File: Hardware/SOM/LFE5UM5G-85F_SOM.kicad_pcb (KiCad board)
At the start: 8 copper layers, 67.6 x 25.4 mm, 157 parts, among them J1 SODIMM-200_Split, U1 LFE5UM5G-85F, U2 AS4C256M16D3, U3 W25Q128JVP, U4 TPS62A02ADRL, U5 TPS62A02ADRL, U6 TPS62A02ADRL, U7 TPS62A02ADRL

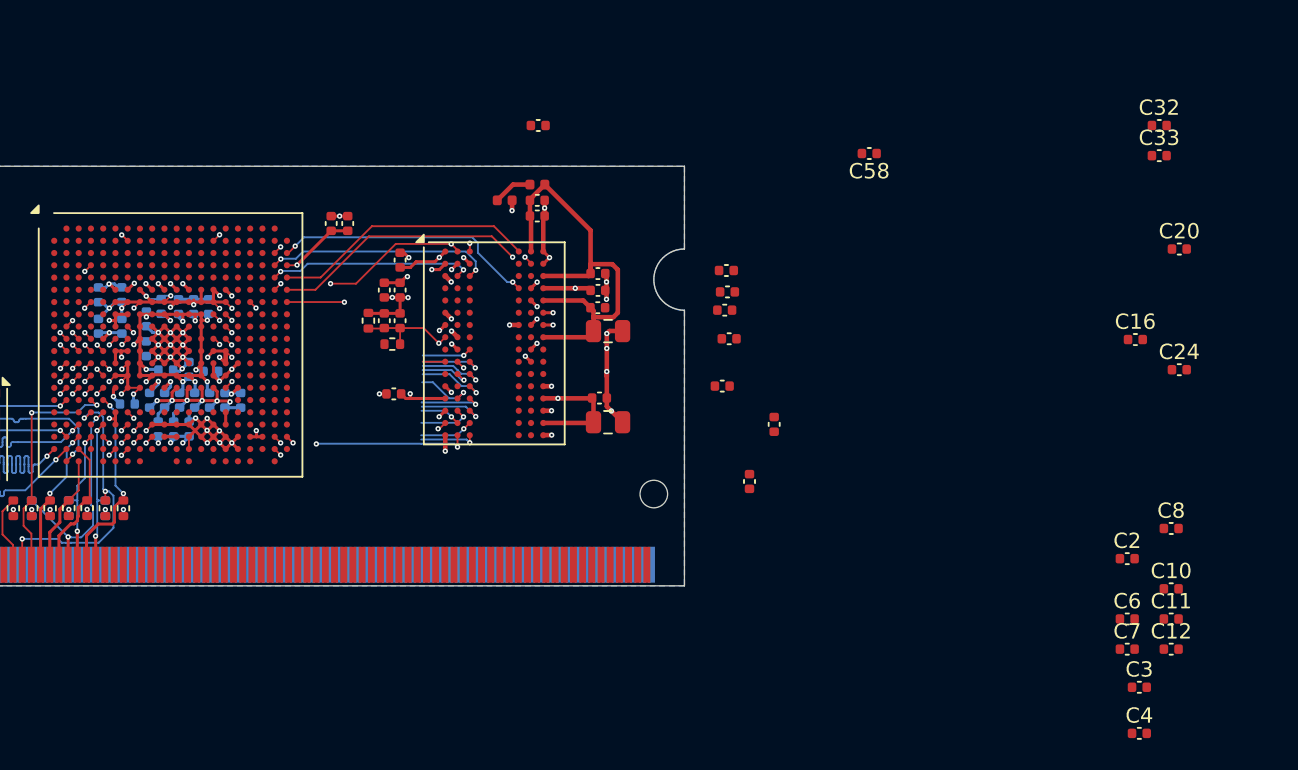
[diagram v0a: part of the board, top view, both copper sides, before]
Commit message: SOM: decoupling caps placement
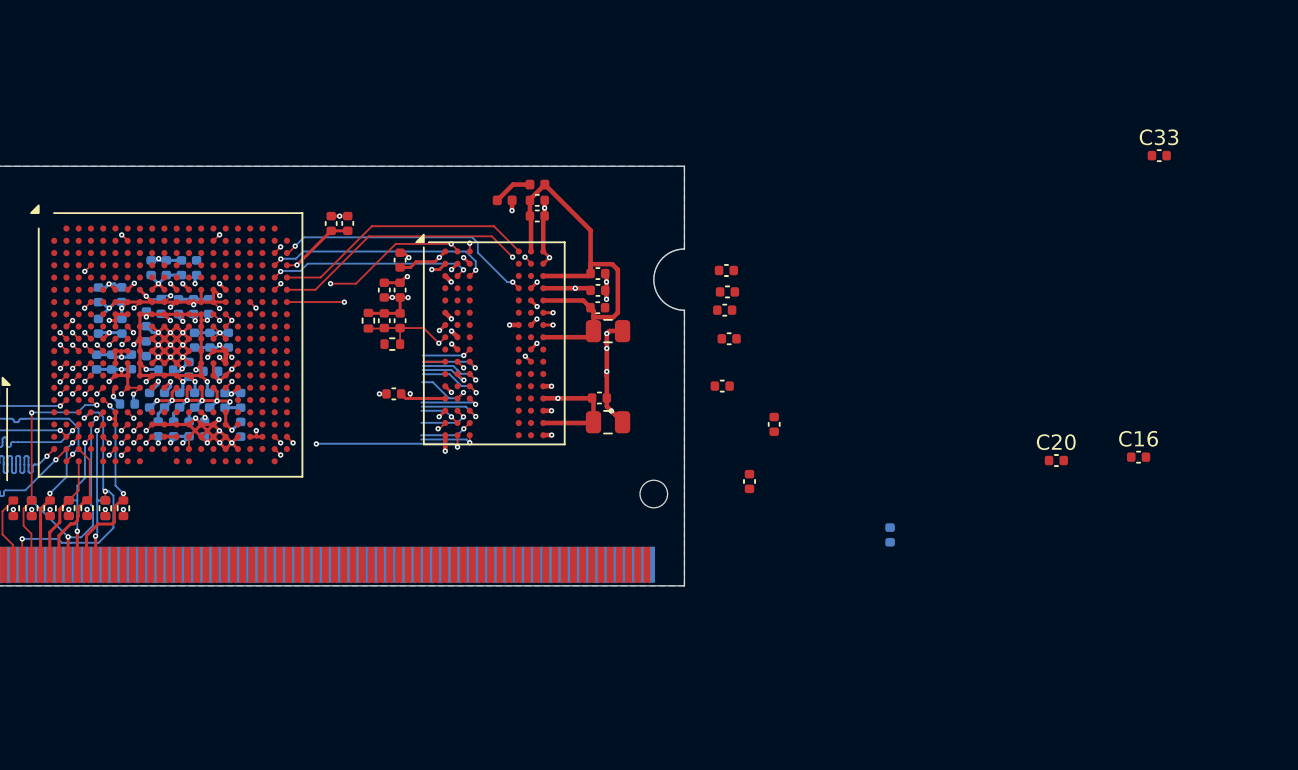
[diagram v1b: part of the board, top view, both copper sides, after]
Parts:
- C10, C11, C12, C2, C24, C3, C32, C4, C56, C58, C6, C7, C8: moved to B.Cu
- moved C4 72.3 mm to (111.1, 71.8), turned to 90 degrees
- moved C12 71.7 mm to (112.1, 71.8), turned to 90 degrees
- moved C8 68.8 mm to (113.3, 71.8), turned to 90 degrees
- moved C10 68.0 mm to (116.6, 65.6), turned to -90 degrees
- moved C6 67.8 mm to (114.6, 65.6), turned to -90 degrees
- moved C2 65.6 mm to (115.6, 65.6), turned to -90 degrees
- moved C11 65.4 mm to (118.5, 70.3), turned to -90 degrees
- moved C24 64.5 mm to (117.6, 65.6), turned to -90 degrees
- moved C7 64.2 mm to (117.5, 70.3), turned to -90 degrees
- moved C3 63.7 mm to (119.7, 70.3), turned to -90 degrees
- moved C58 47.0 mm to (118.1, 76.1), turned to 90 degrees
- moved C32 32.0 mm to (162.9, 83.0), turned to -90 degrees
- moved C56 27.8 mm to (120.5, 76.2), turned to 90 degrees
- moved C20 16.0 mm to (173.8, 78.2)
- moved C16 7.68 mm to (179.1, 78.0)
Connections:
- U1 pad L16: unconnected-(U1E-PR50A-PadL16) -> DDR_A4
- U1 pad L17: unconnected-(U1E-PR50B-PadL17) -> DDR_A5
- U1 pad L18: unconnected-(U1E-PR50C-PadL18) -> DDR_A6
- U1 pad L19: unconnected-(U1E-PR47C-PadL19) -> DDR_A2
- U1 pad L20: unconnected-(U1E-PR47A-PadL20) -> DDR_A0
- U1 pad M18: unconnected-(U1E-PR50D-PadM18) -> DDR_A7
- U1 pad M19: unconnected-(U1E-PR47D-PadM19) -> DDR_A3
- U1 pad M20: unconnected-(U1E-PR47B-PadM20) -> DDR_A1
- U1 pad N18: unconnected-(U1E-PR53C-PadN18) -> DDR_A8
- U1 pad P17: unconnected-(U1E-PR53D-PadP17) -> DDR_A9
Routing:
- net 1.5V: track 52.4 -> 61.4 mm, vias 9 -> 10
- net GND: track 208.0 -> 215.9 mm, vias 113 -> 110
- net VCCA1: track 0.80 -> 2.18 mm, vias 0 -> 1
- net 3.3V: track 55.1 -> 54.1 mm, vias 16 -> 15
- net VCC_SER_1: track 0.00 -> 0.81 mm, vias 0 -> 1
- net unconnected-(U1F-PL83B-PadN5): track 0.58 -> 0.00 mm, vias 1 -> 0
- net unconnected-(U1F-PL77A-PadM5): track 0.56 -> 0.01 mm, vias 1 -> 0

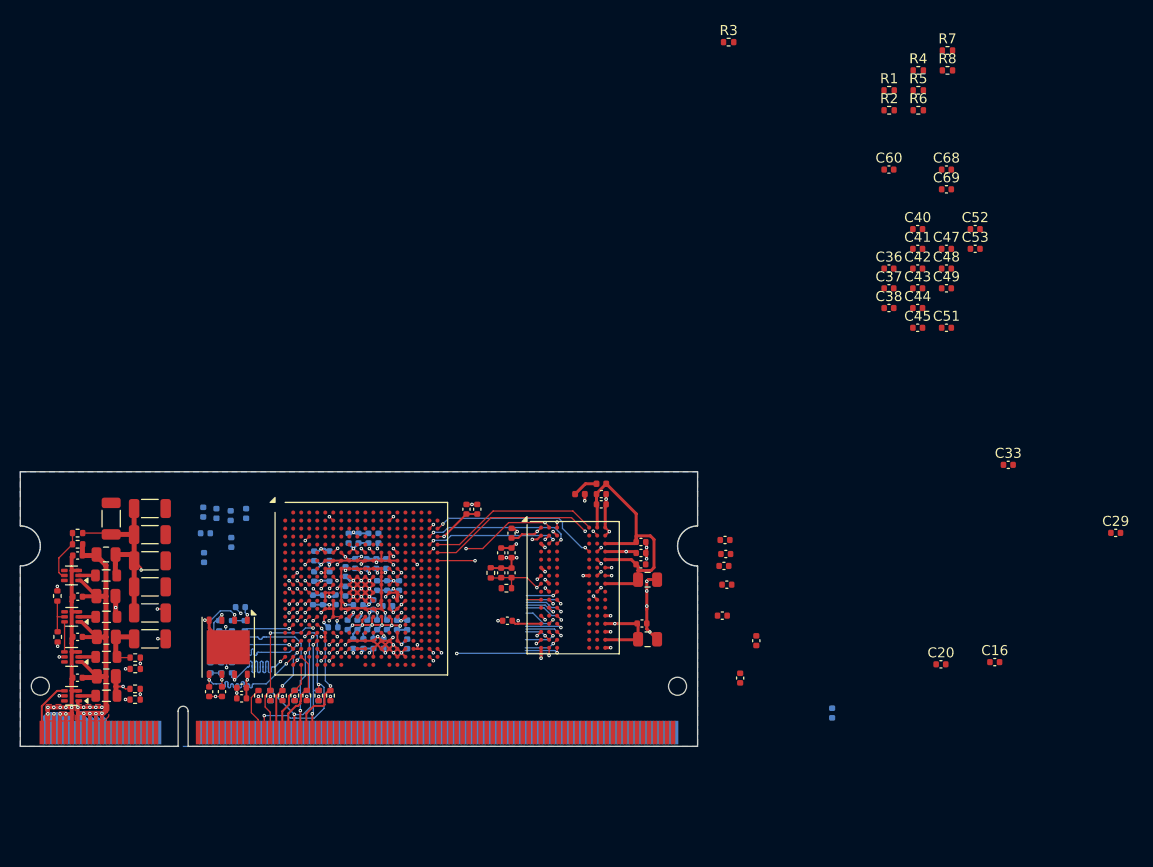
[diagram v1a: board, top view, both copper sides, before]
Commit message: SOM: more caps moved to their place
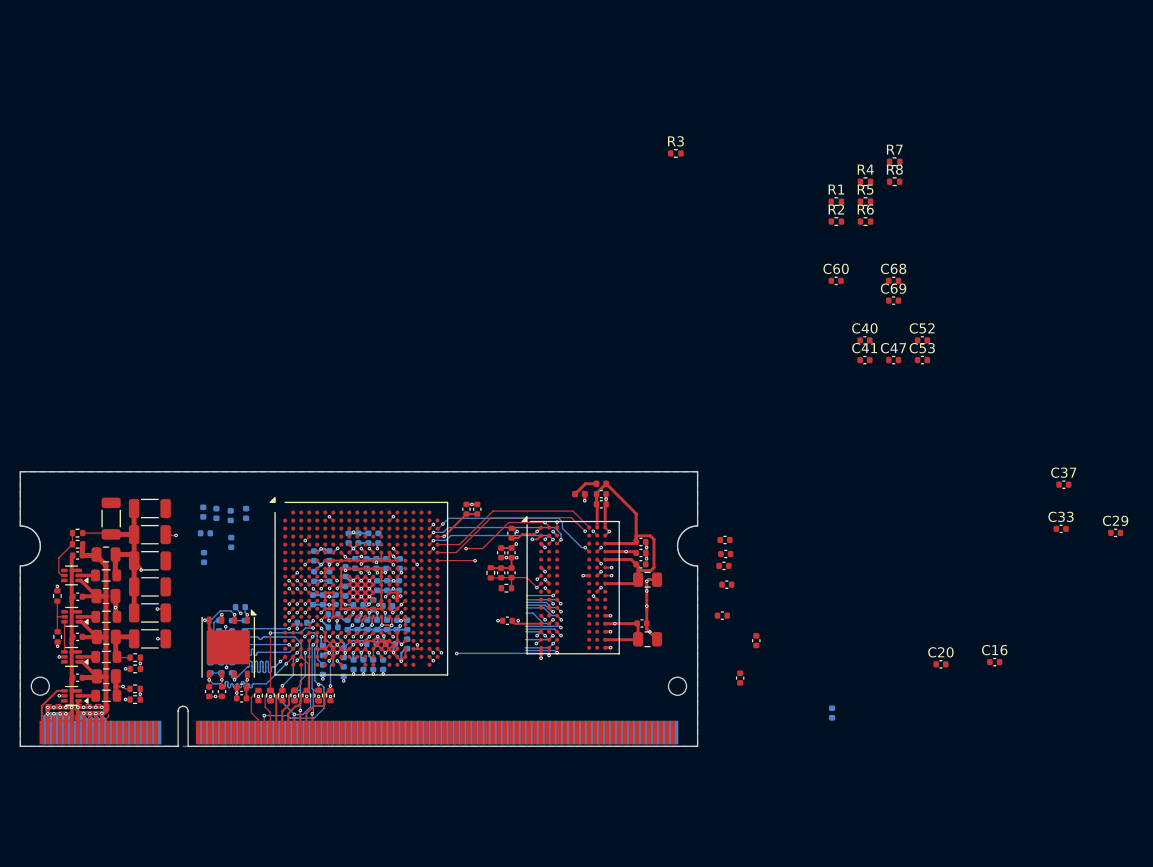
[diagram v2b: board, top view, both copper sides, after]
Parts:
- C36, C38, C42, C43, C44, C45, C48, C49, C51: moved to B.Cu
- moved C42 70.9 mm to (110.0, 74.0)
- moved C43 70.5 mm to (112.1, 78.7), turned to 90 degrees
- moved C51 70.1 mm to (112.1, 76.8), turned to 90 degrees
- moved C48 68.7 mm to (118.1, 78.2), turned to 90 degrees
- moved C44 67.8 mm to (114.2, 78.9), turned to 90 degrees
- moved C49 67.5 mm to (116.9, 76.2), turned to 180 degrees
- moved C45 65.8 mm to (114.2, 77.0), turned to 90 degrees
- moved C38 63.3 mm to (113.1, 73.2)
- moved C36 57.0 mm to (119.8, 68.1), turned to -90 degrees
- moved C37 26.2 mm to (186.0, 60.3)
- moved C68 12.3 mm to (169.0, 39.9)
- moved C40 12.3 mm to (166.2, 45.9)
- moved C41 12.3 mm to (166.2, 47.8)
- moved C47 12.3 mm to (169.0, 47.8)
- moved C52 12.3 mm to (171.9, 45.9)
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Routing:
- net VCCA1: track 2.18 -> 37.7 mm, vias 1 -> 2
- net VCCHTX0: track 0.56 -> 13.0 mm, vias 1 -> 4
- net GND: track 215.9 -> 227.6 mm, vias 110 -> 113
- net VCC_SER_0: track 0.00 -> 9.90 mm, vias 0 -> 3
- net VCC_SER_1: track 0.81 -> 6.57 mm, vias 1 -> 2
- net VCCHTX1: track 0.00 -> 5.43 mm, vias 0 -> 2
- net VCCA0: track 20.1 -> 23.4 mm
- net DDR_VREF: track 26.8 -> 29.9 mm
- net 2.5V_A: track 56.9 -> 59.5 mm
- net 3.3V: track 54.1 -> 55.3 mm
- net unconnected-(U1F-PL83D-PadP5): track 0.58 -> 0.01 mm, vias 1 -> 0
- net unconnected-(U1F-PL92C-PadP3): track 0.57 -> 0.00 mm, vias 1 -> 0
- net unconnected-(U1F-PL92D-PadP4): track 0.57 -> 0.02 mm, vias 1 -> 0

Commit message: Decopuling placement continued
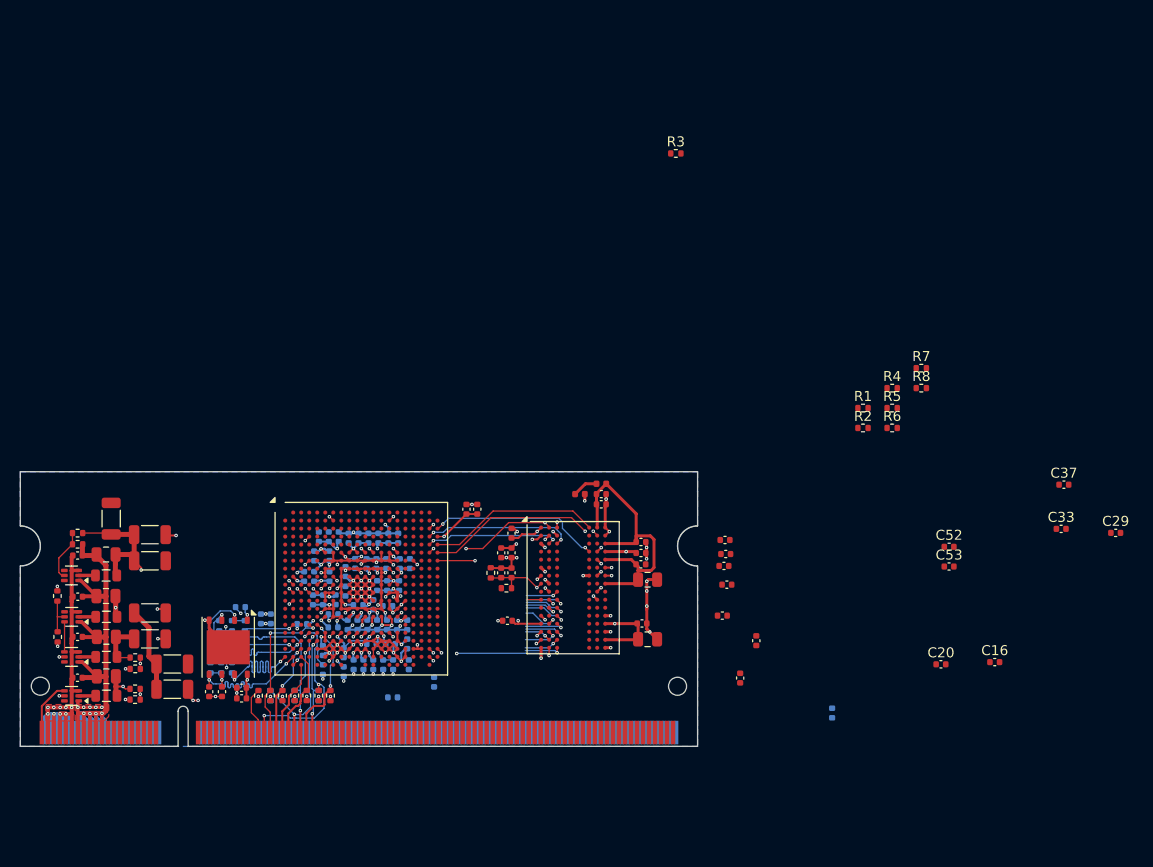
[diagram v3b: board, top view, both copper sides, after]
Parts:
- C40, C41, C47, C60, C68, C69: moved to B.Cu
- moved C47 68.2 mm to (105.9, 73.7), turned to -90 degrees
- moved C40 65.5 mm to (106.9, 73.7), turned to -90 degrees
- moved C69 63.8 mm to (119.0, 81.5), turned to 180 degrees
- moved C68 60.9 mm to (123.2, 80.0), turned to 90 degrees
- moved C60 57.3 mm to (120.7, 78.2), turned to 90 degrees
- moved C41 56.1 mm to (119.1, 78.2), turned to 90 degrees
- moved C53 20.8 mm to (174.6, 68.4)
- moved R7 20.8 mm to (171.8, 48.6)
- moved R8 20.8 mm to (171.8, 50.6)
- moved R1 20.8 mm to (166.0, 52.6)
- moved R2 20.8 mm to (166.0, 54.6)
- moved R5 20.8 mm to (168.9, 52.6)
- moved R6 20.8 mm to (168.9, 54.6)
- moved R4 20.8 mm to (168.9, 50.6)
- moved C52 20.8 mm to (174.6, 66.5)
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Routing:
- net VCCHTX0: track 13.0 -> 33.4 mm, vias 4 -> 6
- net 3.3V: track 55.3 -> 66.1 mm, vias 15 -> 17
- net GND: track 227.6 -> 234.7 mm, vias 113 -> 115
- net VCCA0: track 23.4 -> 24.6 mm, vias 2 -> 3
- net 1.5V: track 61.7 -> 62.7 mm
- net 1.2V: track 74.0 -> 74.8 mm
- net unconnected-(U1F-PL89A-PadN2): track 0.58 -> 0.00 mm, vias 1 -> 0
- net unconnected-(U1F-PL92B-PadP2): track 0.57 -> 0.00 mm, vias 1 -> 0
- net unconnected-(U1F-PL56A-PadK4): track 0.57 -> 0.00 mm, vias 1 -> 0
- net unconnected-(U1F-PL50D-PadK3): track 0.57 -> 0.00 mm, vias 1 -> 0
- net unconnected-(U1F-PL86A-PadN3): track 0.56 -> 0.00 mm, vias 1 -> 0
- net unconnected-(U1F-PL83C-PadN4): track 0.56 -> 0.00 mm, vias 1 -> 0
- net unconnected-(U1F-PL86B-PadM3): track 0.53 -> 0.00 mm, vias 1 -> 0
- net unconnected-(U1F-PL83A-PadM4): track 0.53 -> 0.00 mm, vias 1 -> 0

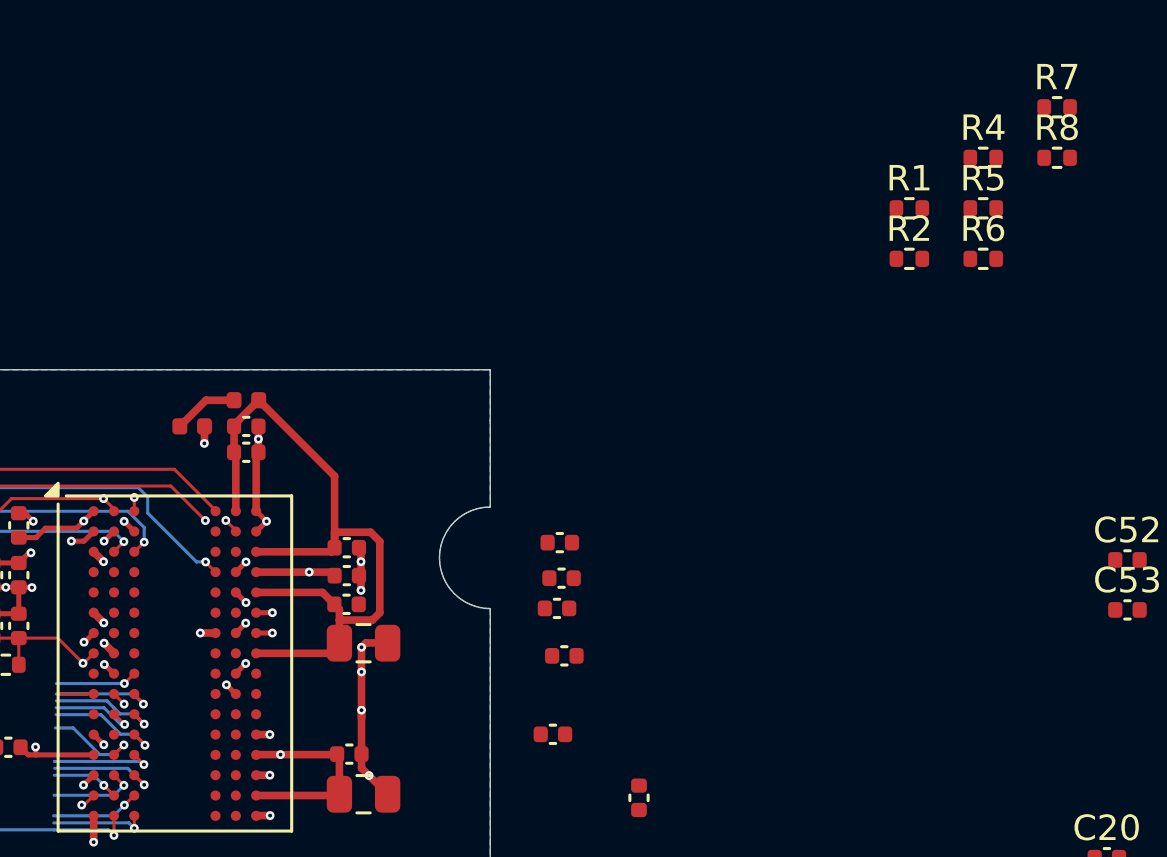
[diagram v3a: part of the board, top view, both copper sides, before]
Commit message: DDR clock schematics fixed
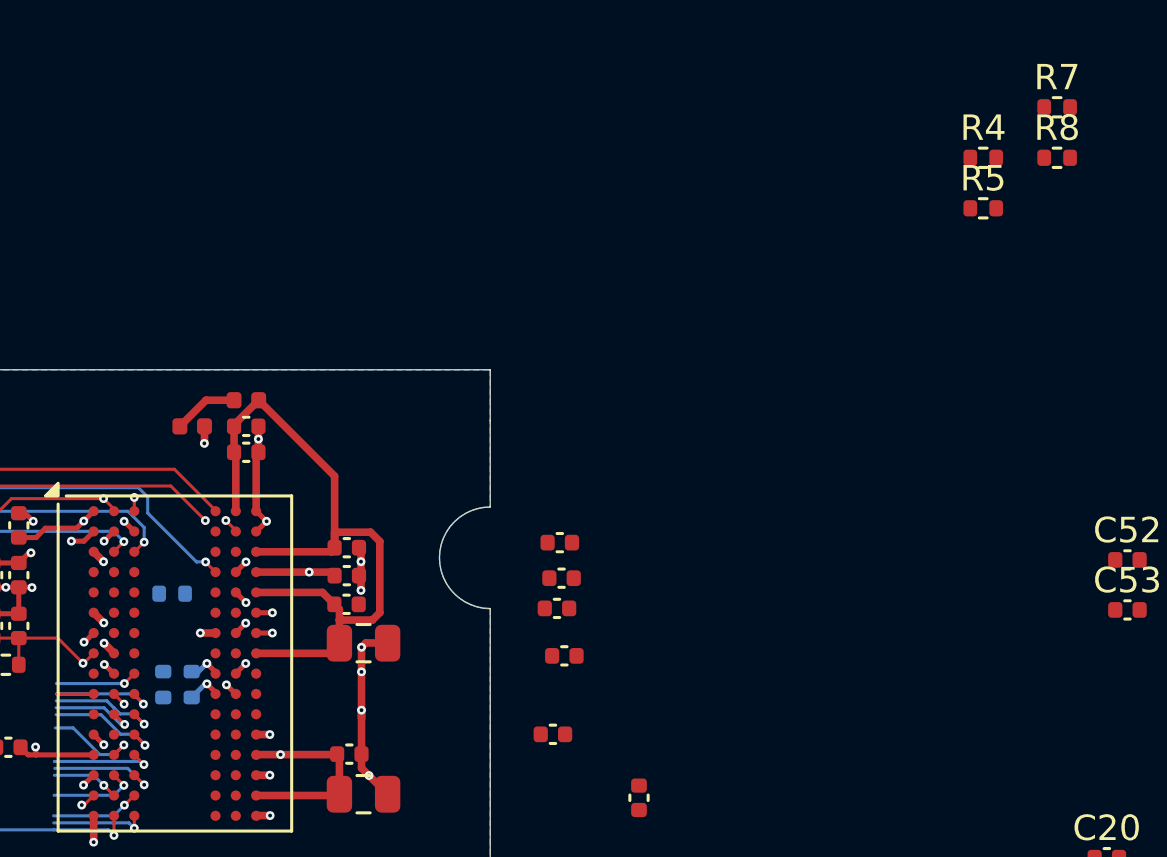
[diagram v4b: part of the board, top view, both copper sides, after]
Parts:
- R1, R2, R6: moved to B.Cu
- moved R6 36.4 mm to (136.6, 71.4), turned to 90 degrees
- moved R1 33.9 mm to (137.7, 71.4), turned to -90 degrees
- moved R2 31.9 mm to (136.9, 67.8)
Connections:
- R1 pad 1: /DDR/DDR_CKE -> DDR_CK_P
- R1 pad 2: /DDR/DDR_NCK -> DDR_CK_N
- U2 pad J7: DDR_CK -> DDR_CK_P
- U2 pad K9: DDR_CK_P -> DDR_CKE
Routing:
- net DDR_CK_N: track 0.00 -> 1.36 mm, vias 0 -> 1
- net DDR_CK_P: track 0.00 -> 1.27 mm, vias 0 -> 1
